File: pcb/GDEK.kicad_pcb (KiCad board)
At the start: 2 copper layers, 276 x 118 mm, 326 parts, among them J1 TYPE-C-31-M-13C, J101 TYPE-C-31-M-13C, J102 AudioJack4, J103 Debug pads, J2 AudioJack4, J3 Debug pads, SW1 SW_Push_45deg, SW10 SW_Push_45deg, SW101 SW_Push_45deg, SW102 SW_Push_45deg, SW103 SW_Push_45deg, SW104 SW_Push_45deg, SW105 SW_Push_45deg, SW106 SW_Push_45deg, SW107 SW_Push_45deg, SW108 SW_Push_45deg, SW109 SW_Push_45deg, SW11 SW_Push_45deg, SW110 SW_Push_45deg, SW111 SW_Push_45deg, SW112 SW_Push_45deg, SW113 SW_Push_45deg, SW114 SW_Push_45deg, SW115 SW_Push_45deg, SW116 SW_Push_45deg, SW117 SW_Push_45deg, SW118 SW_Push_45deg, SW119 SW_Push_45deg, SW12 SW_Push_45deg, SW120 SW_Push_45deg, SW121 SW_Push_45deg, SW122 SW_Push_45deg, SW123 SW_Push_45deg, SW124 SW_Push_45deg, SW125 SW_Push_45deg, SW126 SW_Push_45deg, SW127 SW_Push_45deg, SW128 SW_Push_45deg, SW129 SW_Push_45deg, SW13 SW_Push_45deg, SW130 SW_Push_45deg, SW131 RotaryEncoder_Switch, SW14 SW_Push_45deg, SW15 SW_Push_45deg, SW16 SW_Push_45deg, SW17 SW_Push_45deg, SW18 SW_Push_45deg, SW19 SW_Push_45deg, SW2 SW_Push_45deg, SW20 SW_Push_45deg, SW21 SW_Push_45deg, SW22 SW_Push_45deg, SW23 SW_Push_45deg, SW24 SW_Push_45deg, SW25 SW_Push_45deg, SW26 SW_Push_45deg, SW27 SW_Push_45deg, SW28 SW_Push_45deg, SW29 SW_Push_45deg, SW3 SW_Push_45deg, SW30 SW_Push_45deg, SW31 RotaryEncoder_Switch, SW4 SW_Push_45deg, SW5 SW_Push_45deg, SW6 SW_Push_45deg, SW7 SW_Push_45deg, SW8 SW_Push_45deg, SW9 SW_Push_45deg, U1 RP2040, U101 RP2040, U102 W25Q128JVS, U103 74AHCT1G125, U104 USBLC6-2P6, U105 XC6210B332MR, U2 W25Q128JVS, U3 74AHCT1G125, U4 USBLC6-2P6, U5 XC6210B332MR, Y1 ABM8-272-T3, Y101 ABM8-272-T3

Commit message: 🚧 Place LEDs
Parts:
- moved LD106 256.9 mm to (191.5, 36.2)
- moved LD112 241.9 mm to (191.5, 55.2)
- moved LD105 238.6 mm to (210.5, 32.8)
- moved LD118 227.7 mm to (191.5, 74.8)
- moved LD130 224.1 mm to (172.2, 97.8)
- moved LD111 223.2 mm to (210.5, 51.8)
- moved LD104 220.4 mm to (229.5, 29.2)
- moved LD129 215.5 mm to (178.2, 124.2)
- moved LD124 214.6 mm to (191.8, 93.0)
- moved LD117 208.6 mm to (210.8, 71.0)
- moved LD110 204.7 mm to (229.5, 48.2)
- moved LD128 201.3 mm to (192.7, 113.8)
- moved LD103 199.3 mm to (248.5, 32.8)
- moved LD123 194.7 mm to (211.8, 89.0)
- moved LD116 190.2 mm to (229.0, 68.5)
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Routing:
- added copper zone on B.Cu, net GND_R
- added copper zone on F.Cu, net GND_R

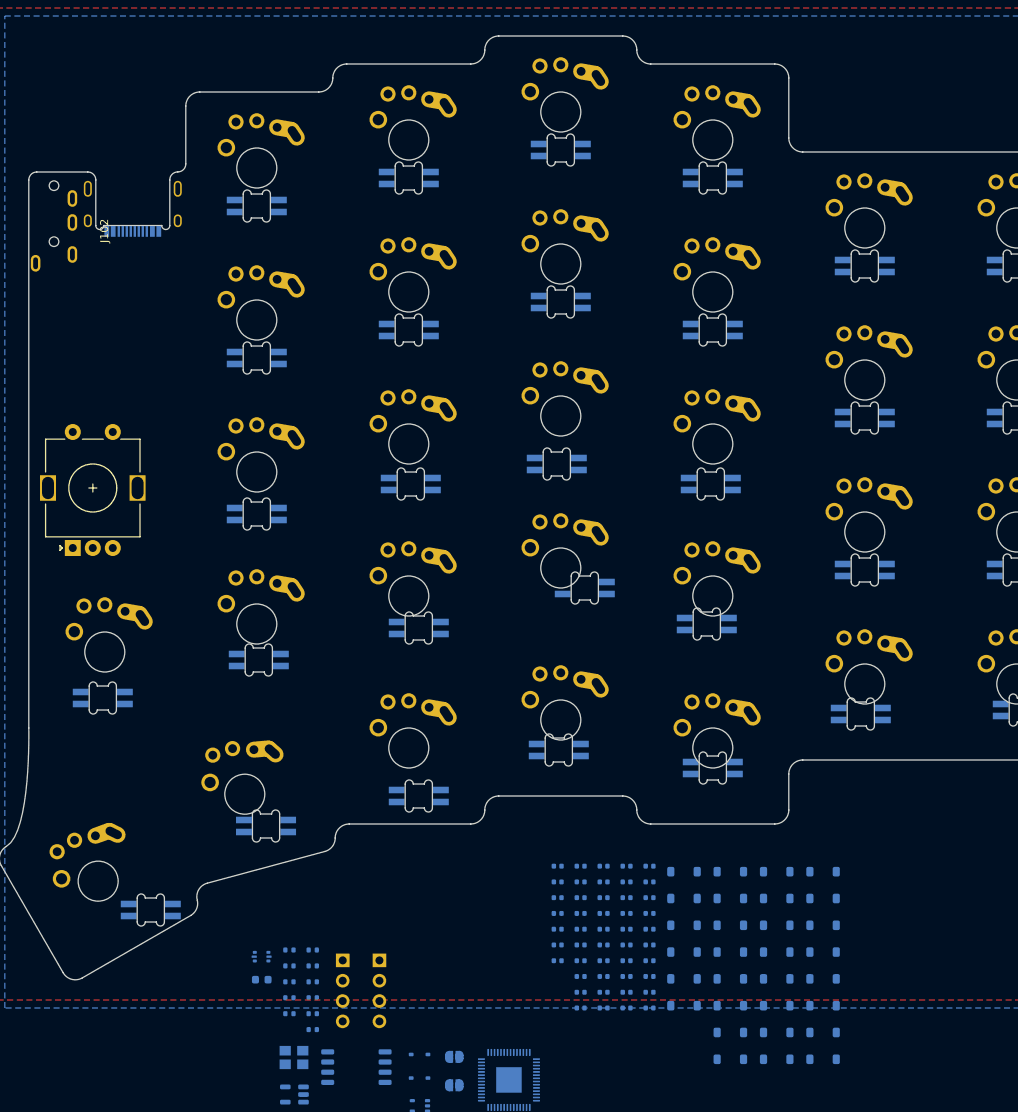
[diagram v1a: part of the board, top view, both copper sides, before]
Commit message: ✨ Right hand: place diodes
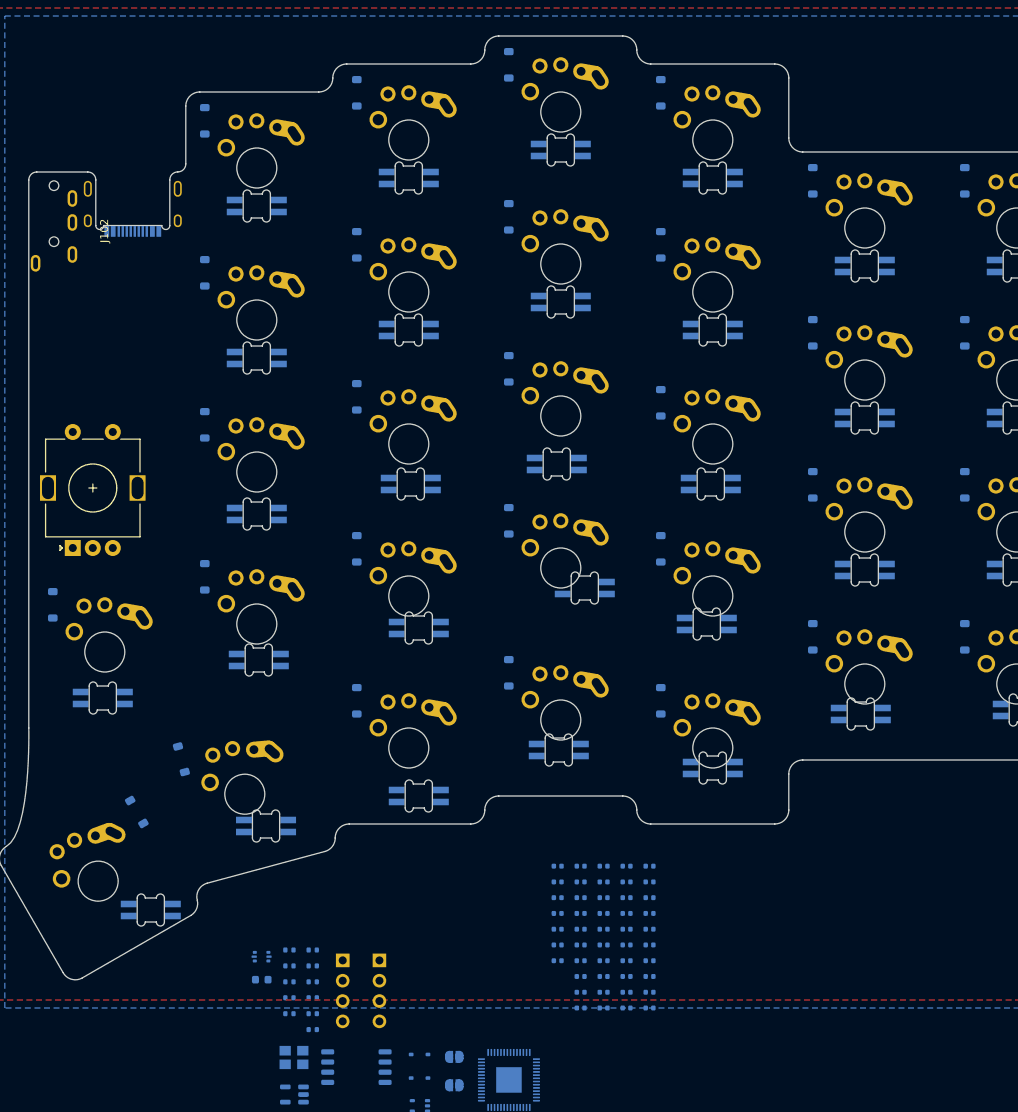
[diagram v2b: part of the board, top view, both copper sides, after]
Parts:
- moved D106 134.9 mm to (185.0, 25.6), turned to -90 degrees
- moved D105 125.2 mm to (204.0, 22.1), turned to -90 degrees
- moved D104 117.7 mm to (223.0, 18.6), turned to -90 degrees
- moved D112 111.0 mm to (185.0, 44.6), turned to -90 degrees
- moved D103 106.0 mm to (242.0, 22.1), turned to -90 degrees
- moved D111 100.0 mm to (204.0, 41.1), turned to -90 degrees
- moved D130 93.5 mm to (166.0, 86.1), turned to -90 degrees
- moved D116 92.6 mm to (223.0, 56.6), turned to -90 degrees
- moved D110 91.6 mm to (223.0, 37.6), turned to -90 degrees
- moved D108 90.8 mm to (261.0, 52.1), turned to -90 degrees
- moved D102 89.7 mm to (261.0, 33.1), turned to -90 degrees
- moved D107 89.2 mm to (280.0, 52.1), turned to -90 degrees
- moved D124 89.2 mm to (185.0, 82.6), turned to -90 degrees
- moved D118 88.4 mm to (185.0, 63.6), turned to -90 degrees
- moved D101 88.2 mm to (280.0, 33.1), turned to -90 degrees
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
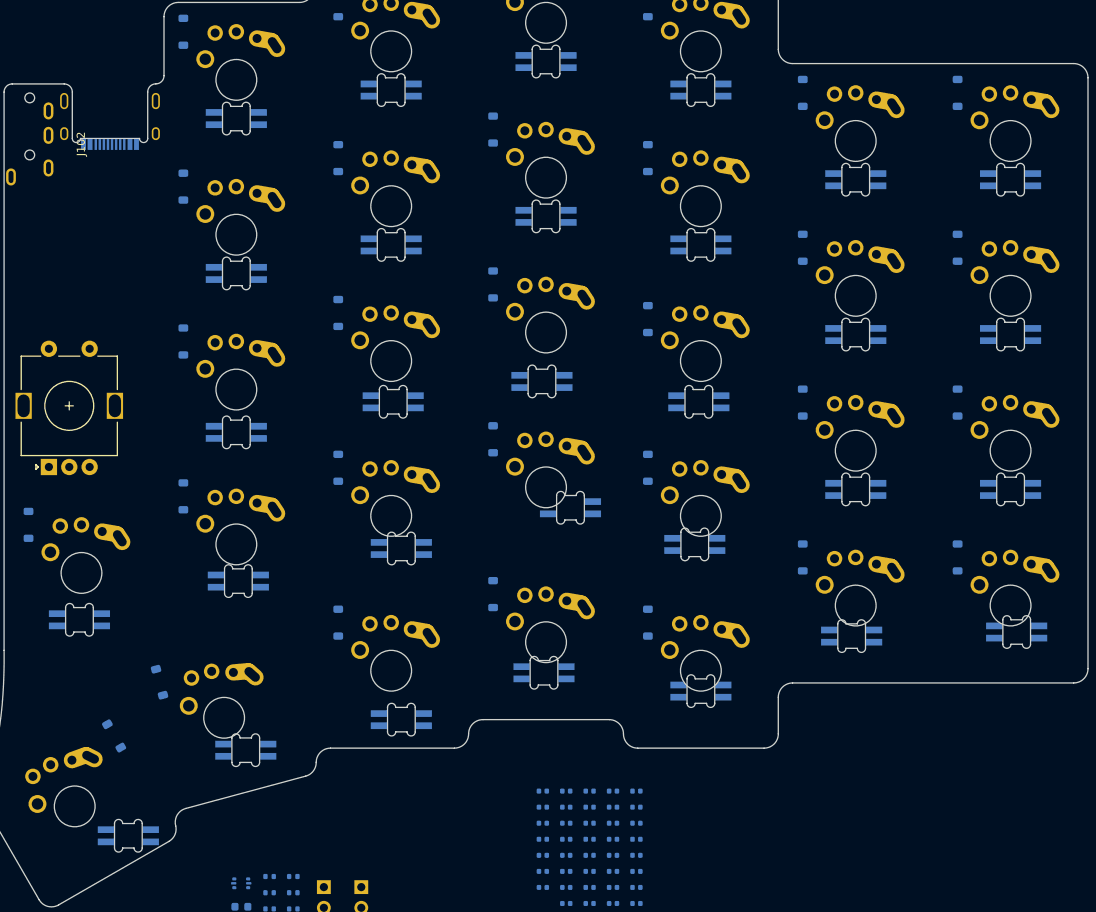
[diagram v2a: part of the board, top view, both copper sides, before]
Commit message: ✨ Right hand: finish LEDs positioning
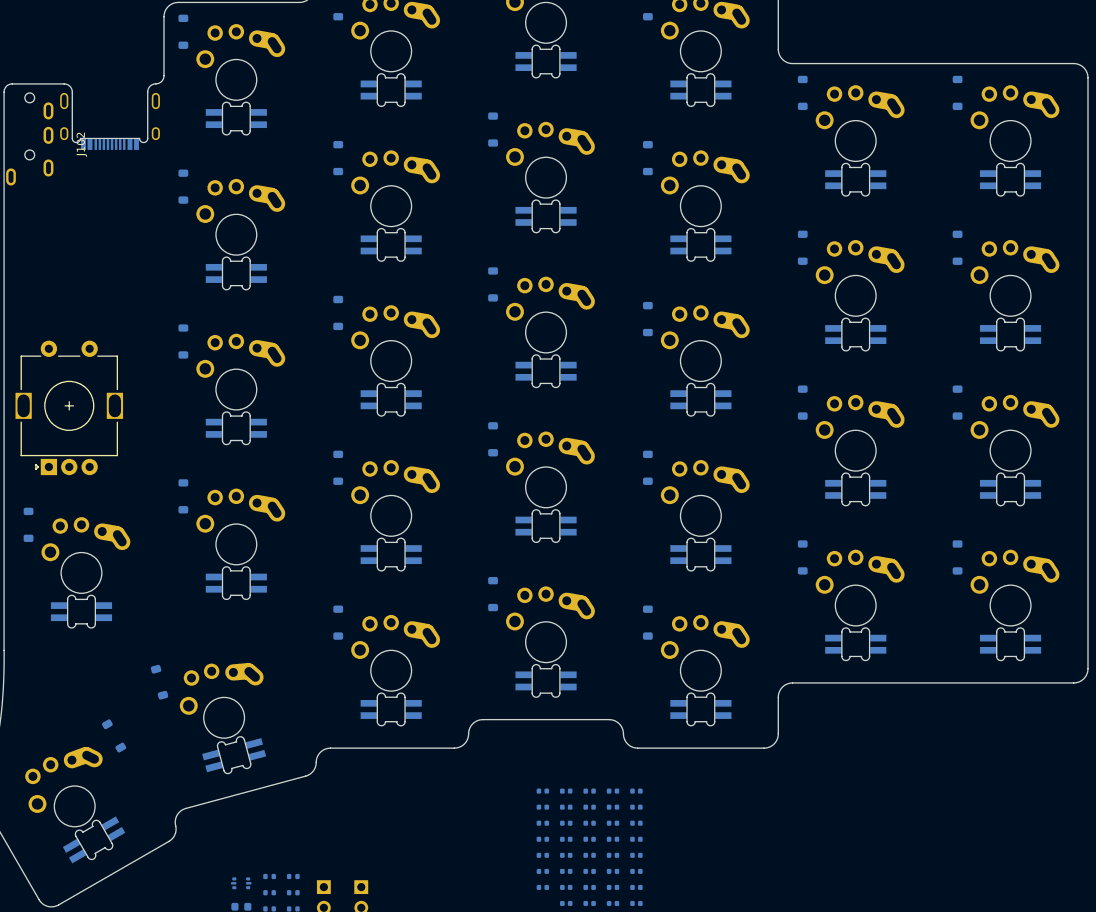
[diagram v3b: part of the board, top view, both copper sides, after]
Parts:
- moved LD129 4.24 mm to (174.0, 124.8), turned to 30 degrees
- moved LD122 3.75 mm to (229.5, 86.2)
- moved LD125 2.25 mm to (248.5, 108.8), turned to 0 degrees
- moved LD127 1.77 mm to (210.5, 108.8), turned to 0 degrees
- moved LD119 1.68 mm to (286.5, 100.8)
- moved LD128 1.55 mm to (191.2, 114.4), turned to 15 degrees
- moved LD121 1.46 mm to (248.5, 89.8)
- moved LD123 1.46 mm to (210.5, 89.8)
- moved LD116 1.35 mm to (229.5, 67.2), turned to 0 degrees
- moved LD120 1.12 mm to (267.5, 100.8)
- moved LD126 1.03 mm to (229.5, 105.2), turned to 0 degrees
- moved LD130 1.03 mm to (172.5, 96.8)
- moved LD118 0.50 mm to (191.5, 74.2), turned to 0 degrees
- moved LD115 0.35 mm to (248.5, 70.8), turned to 0 degrees
- moved LD117 0.35 mm to (210.5, 70.8), turned to 0 degrees
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
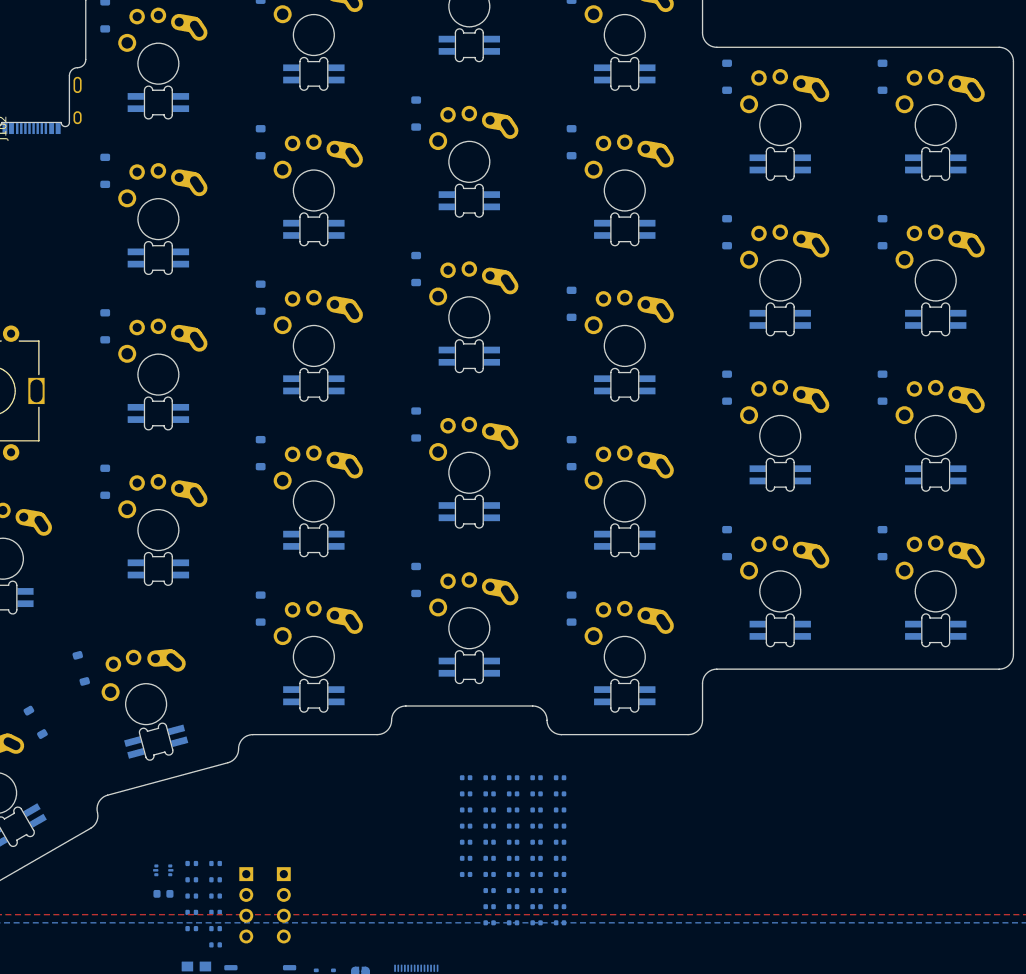
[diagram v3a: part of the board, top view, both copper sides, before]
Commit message: ✨ Right hand: place decoupling capacitors of LEDs
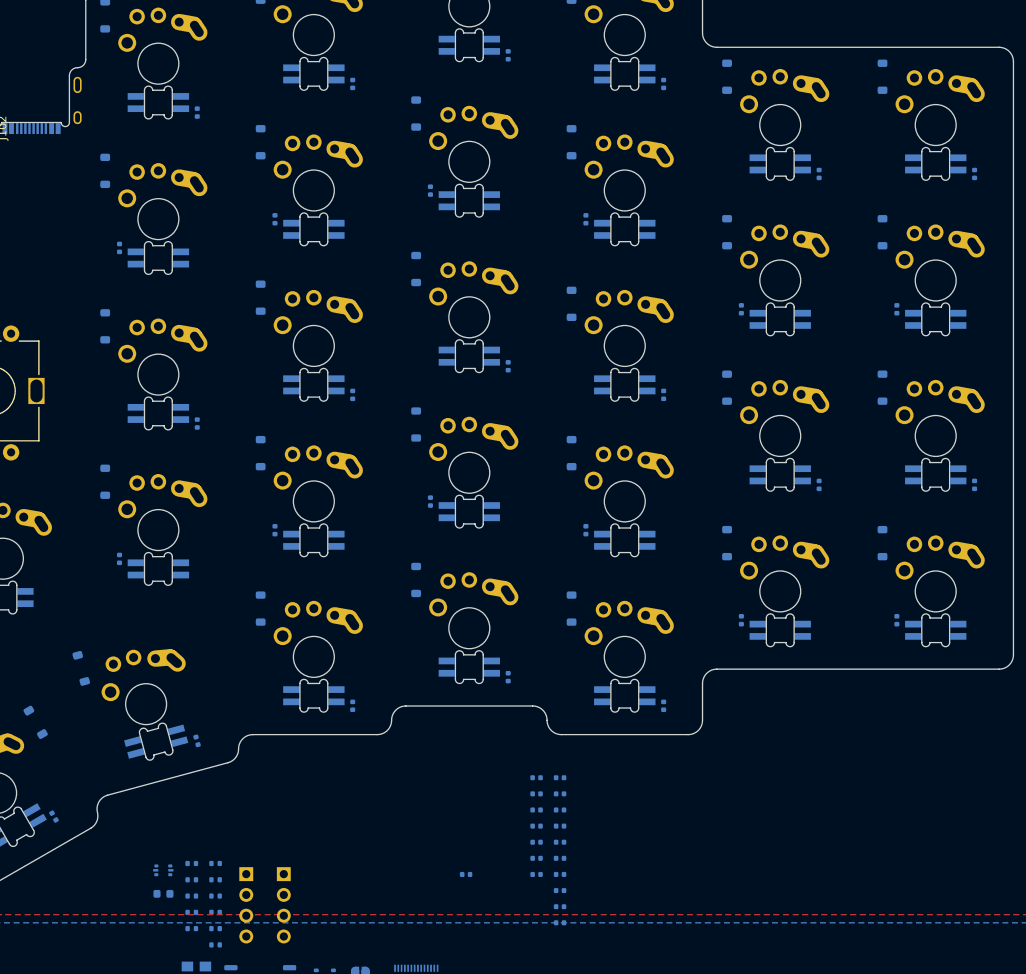
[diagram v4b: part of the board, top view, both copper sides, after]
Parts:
- moved C120 103.7 mm to (253.2, 34.0), turned to 90 degrees
- moved C118 102.6 mm to (291.2, 45.0), turned to 90 degrees
- moved C119 96.0 mm to (272.2, 45.0), turned to 90 degrees
- moved C129 93.8 mm to (186.8, 54.0), turned to -90 degrees
- moved C123 93.6 mm to (196.2, 37.5), turned to 90 degrees
- moved C122 88.9 mm to (215.2, 34.0), turned to 90 degrees
- moved C121 88.3 mm to (234.2, 30.5), turned to 90 degrees
- moved C128 87.0 mm to (205.8, 50.5), turned to -90 degrees
- moved C127 84.2 mm to (224.8, 47.0), turned to -90 degrees
- moved C124 78.7 mm to (281.8, 61.5), turned to -90 degrees
- moved C126 78.6 mm to (243.8, 50.5), turned to -90 degrees
- moved C130 77.8 mm to (291.2, 83.0), turned to 90 degrees
- moved C125 70.9 mm to (262.8, 61.5), turned to -90 degrees
- moved C135 62.4 mm to (196.2, 75.5), turned to 90 degrees
- moved C136 57.7 mm to (281.8, 99.5), turned to -90 degrees
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
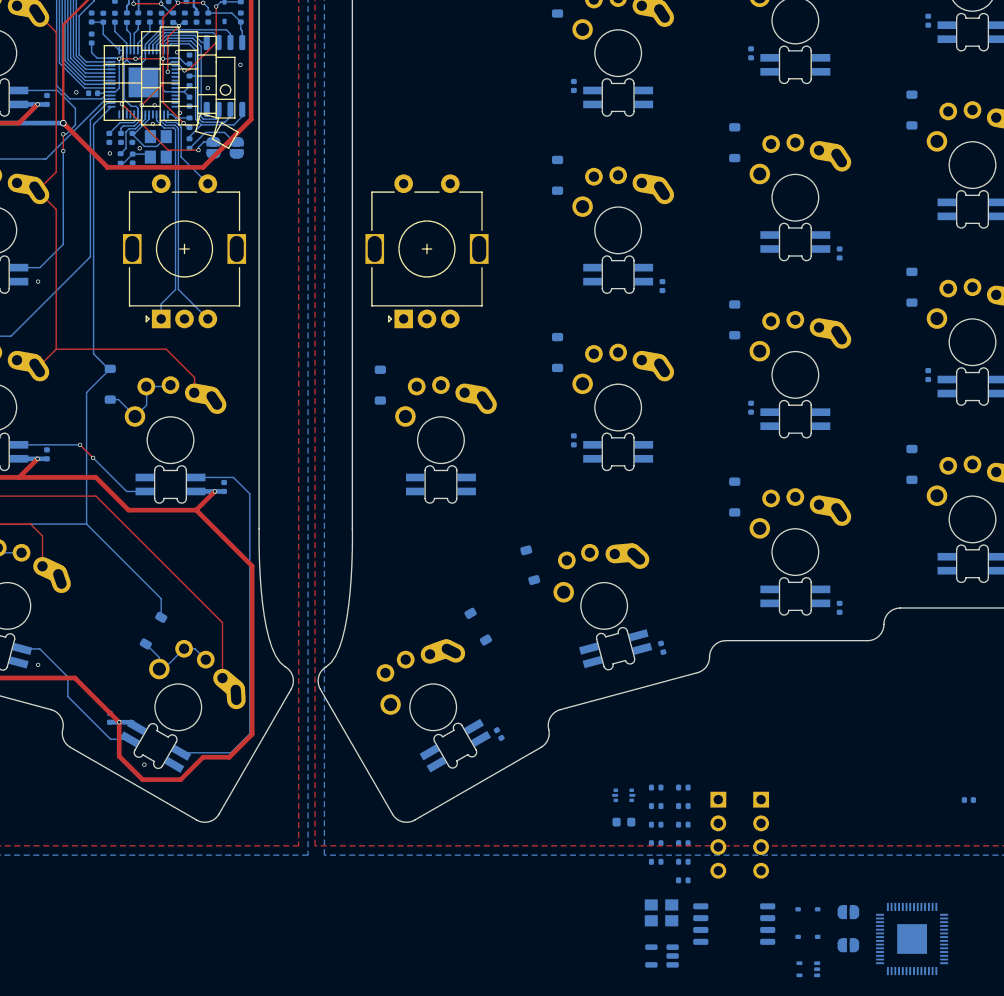
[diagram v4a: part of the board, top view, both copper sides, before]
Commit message: 🎨 Set all capacitors in the same orientation
There was one remaining horizontal one.
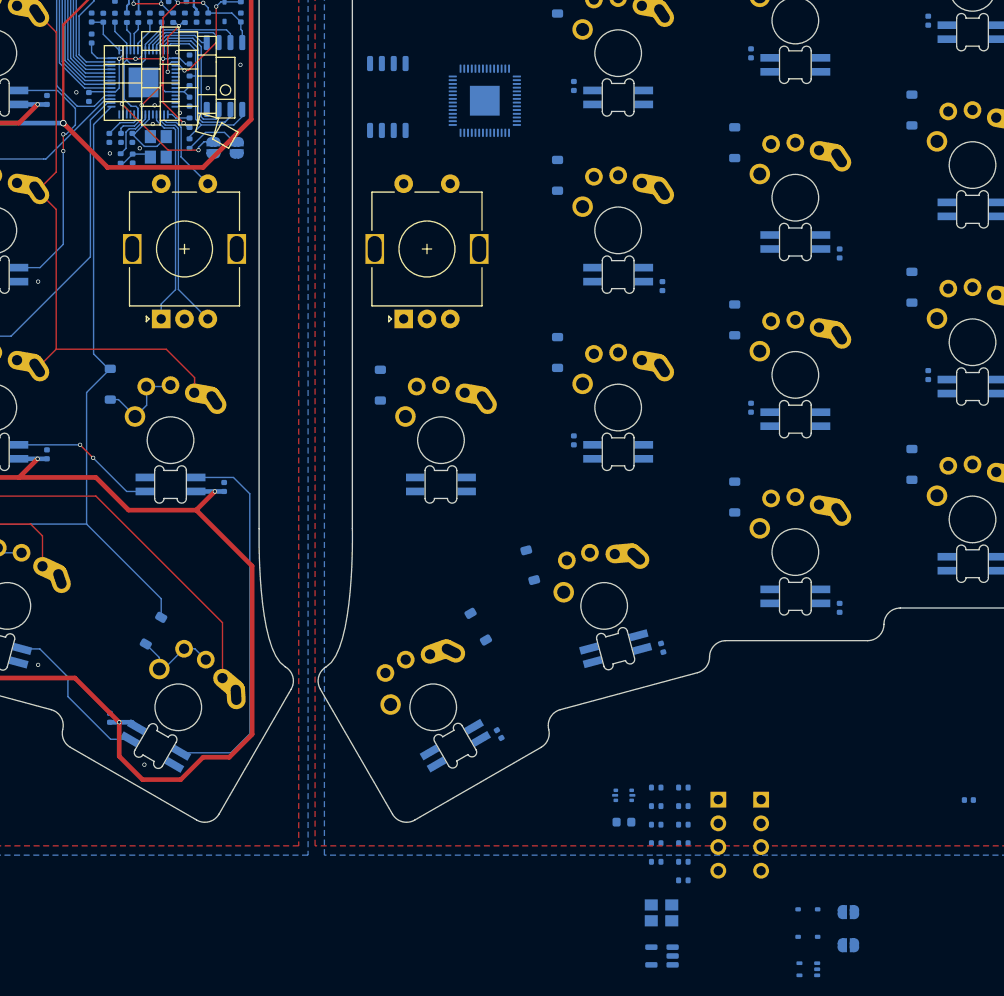
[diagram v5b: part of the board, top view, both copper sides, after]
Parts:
- moved U101 100.9 mm to (177.2, 55.6)
- moved U102 96.2 mm to (166.8, 55.2), turned to -90 degrees
- moved C13 0.60 mm to (134.8, 55.2), turned to -90 degrees
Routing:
- net +3V3: track 72.7 -> 73.6 mm
- net /ROW1: track 133.8 -> 134.5 mm
